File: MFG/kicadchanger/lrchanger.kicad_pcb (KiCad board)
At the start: 2 copper layers, 99.1 x 81.3 mm, 31 parts, among them J1 INPUTS, J2 UI_OUTPUTS, J3 IBUS, J4 RIGHT+, J5 RIGHT-, J6 LEFT+, J7 LEFT-, J8 POWER, K1 G2RK-2, K2 G2RK-2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

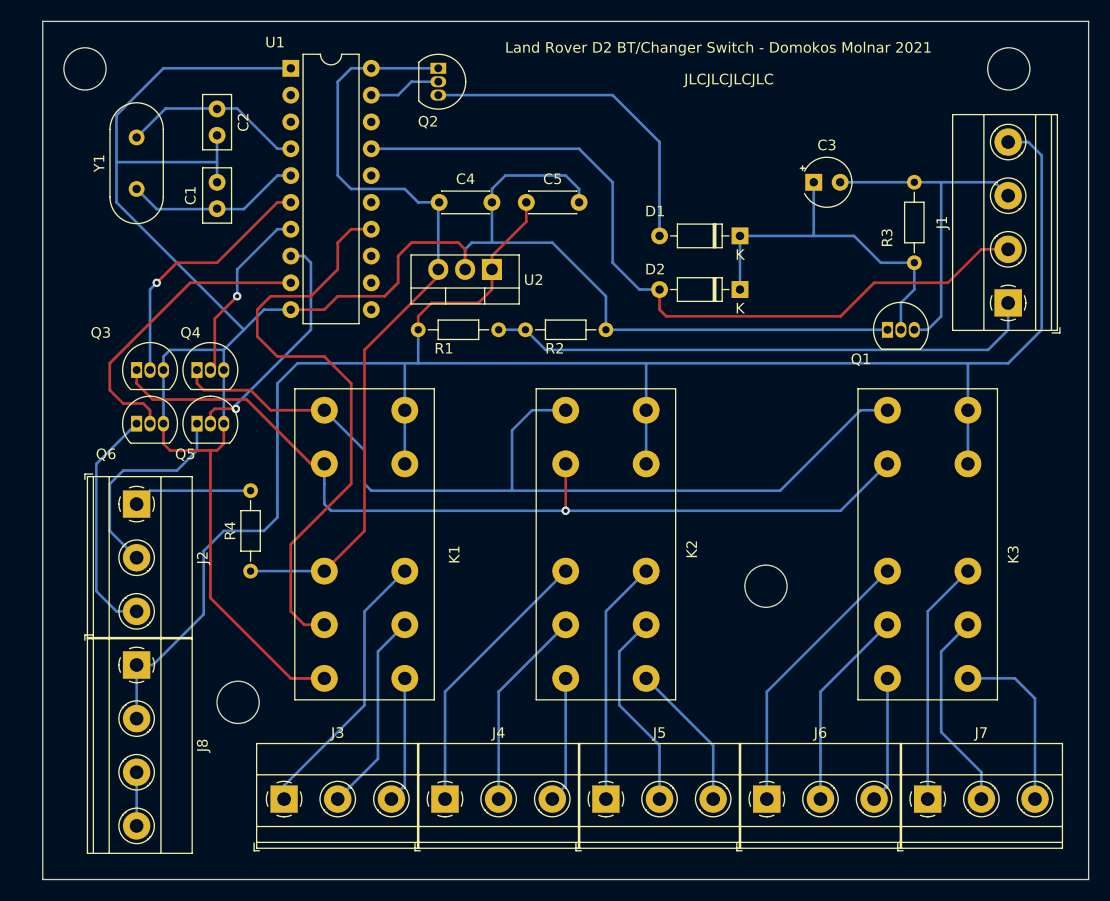
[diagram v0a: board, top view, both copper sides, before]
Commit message: Simulate poweroff and modify design
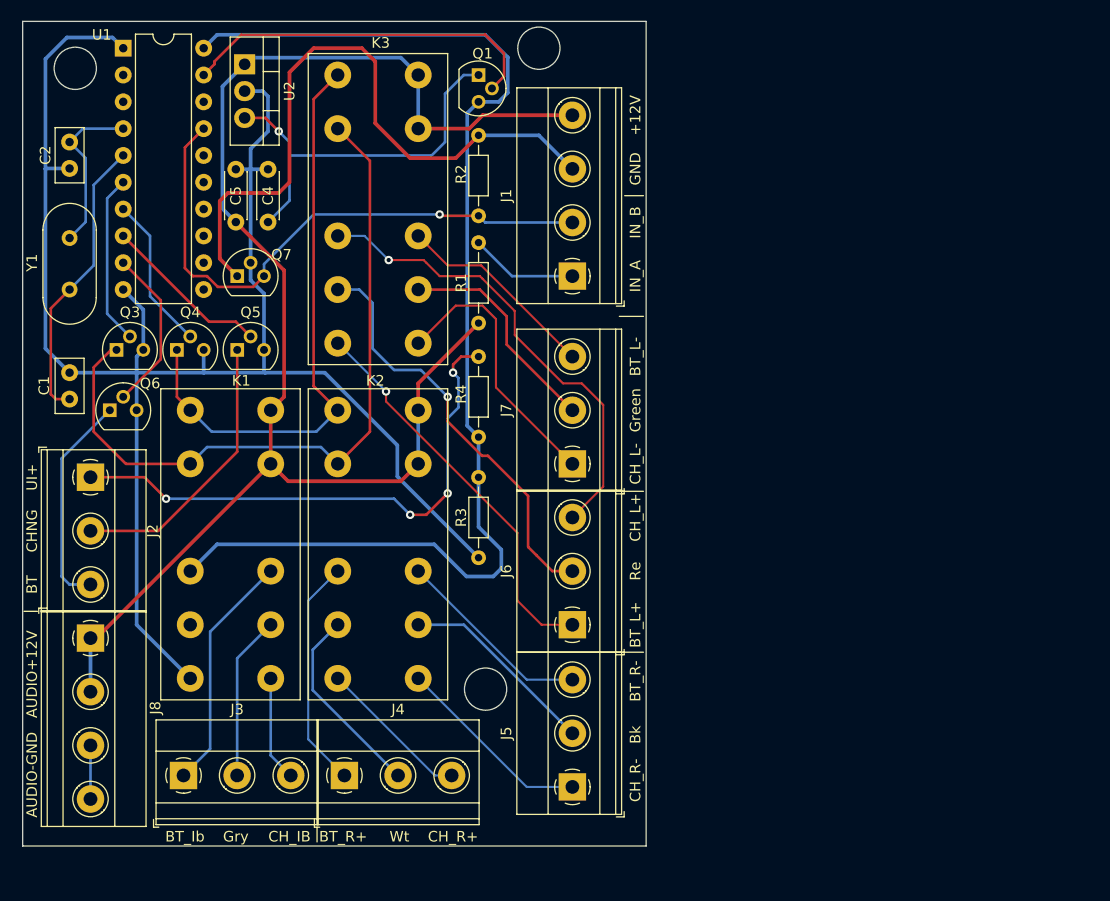
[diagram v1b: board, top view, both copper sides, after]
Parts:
- removed C3: 1u, Capacitor_THT:CP_Radial_Tantal_D4.5mm_P2.50mm
- removed D1, D2: 1N4148, Diode_THT:D_DO-35_SOD27_P7.62mm_Horizontal
- removed Q2: BC327, Package_TO_SOT_THT:TO-92_Inline
- added Q7: 2N5064, Package_TO_SOT_THT:TO-92, F.Cu at (81.9, 87.6)
- Q1, Q3, Q4, Q5, Q6: footprint Package_TO_SOT_THT:TO-92_Inline -> Package_TO_SOT_THT:TO-92
- R1: value 20k -> 5.6k
- R2: value 14k -> 10k
- R3: value 10k -> 500
- R4: value 10R -> 100R
- U1: value AT89C4051 -> AT89C4051-24PU
- U2: value LM7805 -> LM7805_TO220
- Y1: value (none) -> Crystal
- moved K3 61.0 mm to (99.1, 68.6)
- moved R3 49.8 mm to (104.8, 114.3)
- moved J7 46.3 mm to (113.7, 105.4), turned to 90 degrees
- moved Q1 45.6 mm to (104.8, 68.6), turned to -90 degrees
- moved J1 41.4 mm to (113.7, 87.6)
- moved U2 30.4 mm to (82.6, 67.6), turned to -90 degrees
- moved C5 27.6 mm to (81.8, 82.5), turned to 90 degrees
- moved R4 25.0 mm to (104.8, 102.9)
- moved J6 24.7 mm to (113.7, 120.7), turned to 90 degrees
- moved C1 22.8 mm to (66.0, 99.3)
- moved K2 21.6 mm to (99.1, 100.3)
- moved C4 16.3 mm to (84.8, 82.5), turned to 90 degrees
- moved U1 16.0 mm to (71.1, 66.0)
- moved C2 14.3 mm to (66.0, 74.9)
- moved K1 12.7 mm to (85.1, 100.3)
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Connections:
- net Net-(J2-Pad1) renamed /UI+
- net Net-(J2-Pad2) renamed /CHNG
- net Net-(J2-Pad3) renamed /BT
- C4 pad 1: VCC -> Net-(C4-Pad1)
- J5 pad 1: BT_Right- -> CH_Right-
- J5 pad 3: CH_Right- -> BT_Right-
- J6 pad 1: BT_Left+ -> CH_Left+
- J6 pad 3: CH_Left+ -> BT_Left+
- J7 pad 1: BT_Left- -> CH_Left-
- J7 pad 3: CH_Left- -> BT_Left-
- Q1 pad 1: GND -> Net-(C4-Pad1)
- Q1 pad 2: Net-(C3-Pad1) -> PWR_REQ
- Q1 pad 3: GNDPWR -> VCC
- R2 pad 1: INPUT_A -> INPUT_B
- R2 pad 2: GND -> GNDPWR
- R3 pad 1: Net-(C3-Pad1) -> GND
- R3 pad 2: GNDPWR -> VCC
- U1 pad 11: Net-(U1-Pad11) -> unconnected-(U1-Pad11)
- U1 pad 12: Net-(U1-Pad12) -> unconnected-(U1-Pad12)
- U1 pad 13: Net-(U1-Pad13) -> unconnected-(U1-Pad13)
- U1 pad 15: Net-(U1-Pad15) -> unconnected-(U1-Pad15)
- U1 pad 16: Net-(U1-Pad16) -> unconnected-(U1-Pad16)
- U1 pad 18: Net-(U1-Pad18) -> unconnected-(U1-Pad18)
- U1 pad 19: Net-(Q2-Pad2) -> PWR_REQ
- U1 pad 2: Net-(U1-Pad2) -> unconnected-(U1-Pad2)
- U1 pad 3: Net-(U1-Pad3) -> unconnected-(U1-Pad3)
- U2 pad 3: VCC -> Net-(C4-Pad1)
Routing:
- net COIL_STATE: track 56.4 -> 0.00 mm
- net +12V: track 185.8 -> 139.3 mm
- net GND: track 209.4 -> 164.4 mm
- net INPUT_A: track 52.4 -> 10.2 mm
- net /UI+: track 11.3 -> 51.7 mm, vias 0 -> 4
- net VCC: track 76.0 -> 114.8 mm
- net Net-(C4-Pad1): track 0.00 -> 37.4 mm, vias 0 -> 1
- net Net-(C3-Pad1): track 34.6 -> 0.00 mm
- net BT_COIL: track 87.5 -> 55.5 mm
- net GNDPWR: track 32.2 -> 63.2 mm
- net CH_Left+: track 12.0 -> 37.6 mm, vias 0 -> 1
- net Left+_Re: track 19.1 -> 40.0 mm, vias 0 -> 1
- net INPUT_B: track 75.1 -> 55.2 mm, vias 0 -> 1
- net BT_Left+: track 26.3 -> 45.0 mm, vias 0 -> 1
- net CH_COIL: track 85.9 -> 68.9 mm, vias 1 -> 0
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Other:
- board size 99.1 x 81.3 mm -> 59.1 x 78.1 mm
- net class Default removed
- board text added: "+12V"
- board text added: "AUDIO-GND AUDIO+12V"
- board text added: "BT"
- board text added: "BT_Ib"
- board text added: "BT_L+"
- board text added: "BT_L-"
- board text added: "BT_R+"
- board text added: "BT_R-"
- board text added: "Bk"
- board text added: "CHNG"
- board text added: "CH_IB"
- board text added: "CH_L+"
- board text added: "CH_L-"
- board text added: "CH_R+"
- board text added: "CH_R-"
- board text added: "GND"
- board text added: "Green"
- board text added: "Gry"
- board text added: "IBUS"
- board text added: "INPUTS"
- board text added: "IN_A"
- board text added: "IN_B"
- board text added: "LEFT+"
- board text added: "LEFT-"
- board text added: "POWER"
- board text added: "RIGHT+"
- board text added: "RIGHT-"
- board text added: "Re"
- board text added: "UI"
- board text added: "UI+"
- board text added: "Wt"
